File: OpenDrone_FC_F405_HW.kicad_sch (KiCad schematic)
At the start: 88 parts, among them J1 Conn_01x05, J11 Conn_01x05, J12 Conn_01x05, J13 Conn_01x02, J14 Conn_01x02, J16 Conn_01x05, J17 Conn_02x03_Odd_Even, J2 Conn_01x02, J3 Conn_01x02, J4 Conn_01x02, J5 Conn_01x02, J6 Conn_01x08, J7 Conn_01x02, J8 Conn_01x04, J9 Conn_01x02, U1 STM32F405RGTx, U2 TPS54331, U4 MPU6000, U5 HMC5883L, U6 BMP280, U7 TPS54331, U8 Board, Y2 8Mhz

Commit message: update project
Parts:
- added R18: 10k, Resistor_SMD:R_0402_1005Metric, symbol Device:R_Small
- added R19: 470R, Resistor_SMD:R_0402_1005Metric, symbol Device:R_Small
- R14: value 10k -> 0R
- R15: value 3.24k -> 3,3k
- R3: value 10k -> 4,7k
- R5: value 3.24k -> 1k
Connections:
- net 3V3_STEPDOWN: now also R18.2; no longer R14.1
- net 5V_STEPDOWN: now also R19.2; no longer R3.1
- net at R15.1, U2.5 (VSENSE): now also R14.1; no longer R14.2
- net at R5.1, U7.5 (VSENSE): now also R3.1; no longer R3.2
- new net: R14.2, R18.1
- new net: R19.1, R3.2
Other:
- moved on the sheet: C13, C14, C15, C16, C17, C39, C40, C41, D4, J17, L2, R13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

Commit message: update project
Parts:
- removed C20: 100nF, Capacitor_SMD:C_0402_1005Metric, symbol Device:C_Small
- removed C21: 2.2nF, Capacitor_SMD:C_0402_1005Metric, symbol Device:C_Small
- removed J11, J12, J16: Conn_01x05, Footprint:Header_1x05_P2.00mm_Vertical, symbol Connector_Generic:Conn_01x05
- removed J13, J14, J2, J3, J4, J5, J7, J9: Conn_01x02, Footprint:HolePad_1x2, symbol Connector_Generic:Conn_01x02
- removed U4: MPU6000, Footprint:QFN-24-1EP_4x4mm_P0.5mm_EP2.15x2.15mm, symbol MPU6000:MPU6000
- added C8: 10uF, Capacitor_SMD:C_0402_1005Metric, symbol Device:C_Small
- added J10, J11, J12: Conn_01x06, Footprint:Header_1x06_P2.00mm_Vertical, symbol Connector_Generic:Conn_01x06
- added U3: ICM42688, Package_LGA:LGA-14_3x2.5mm_P0.5mm_LayoutBorder3x4y, symbol ICM42688:ICM42688
- C19: value 10nF -> 10uF
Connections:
- net MPU6000_XCL is gone; now on net I2C2_SCL: U5.1 (SCL)
- net MPU6000_XDA is gone; now on net I2C2_SDA: U5.16 (SDA)
- net +3V3: now also R8.2, R9.1, C8.1, J10.6 (Pin_6), U3.5 (VDDIO), U3.8 (VDD); no longer R8.1
- net +5V: now also J12.6 (Pin_6)
- net GND: now also U6.5 (SDO), C8.2, J11.6 (Pin_6), U3.11 (RESV), U3.6 (GND), U3.7 (RESV); no longer R9.2
- net I2C1_SCL: now also J11.2 (Pin_2)
- net I2C1_SDA: now also J11.3 (Pin_3)
- net I2C2_SCL: now also R8.1; no longer R8.2
- net LED_STRIP1: now also J12.2 (Pin_2)
- net LED_STRIP2: now also J12.3 (Pin_3)
- net LORA_IRQ: no longer U1.45 (PA12)
- net LORA_RST: no longer U1.44 (PA11)
- net SPI1_CLK: now also U3.13 (SCL/SCLK)
- net SPI1_CS: now also U3.12 (CS)
- net SPI1_MISO: now also U3.1 (SDO/AD0)
- net SPI1_MOSI: now also U3.14 (SDA/SDIO/SDI)
- net SPI2_CLK: now also J10.5 (Pin_5)
- net SPI2_MISO: now also J10.4 (Pin_4)
- net SPI2_MOSI: now also J10.3 (Pin_3)
- net UART4_RX: now also J12.5 (Pin_5)
- net UART4_TX: now also J12.4 (Pin_4)
- net UART6_RX: now also J10.1 (Pin_1)
- net UART6_TX: now also J10.2 (Pin_2)
- net at U6.2 (CSB): now also R9.2
- net SPI2_CS1: now reaches U1.39 (PC8)
- net SPI2_CS1: now also J11.4 (Pin_4)
- net MPU6000_INT renamed ICM42688_INT
- net ICM42688_INT: now also U3.4 (INT1/INT)
- net SPI2_CS renamed SPI2_CS2
- net SPI2_CS2: now also J11.5 (Pin_5)
- no-connect marks 6 -> 8
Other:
- note added: "ICM42688"
- note added: "QMC5883L"
- note removed: "HMC5883L"
- note removed: "MPU6050"
- moved on the sheet: C18, C22, C23, C24, C25, C26, J6, J8, R7, R8, R9, U5

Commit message: update routing
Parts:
- removed D6: GREEN, LED_SMD:LED_0402_1005Metric, symbol Device:LED_Small
- removed R25: 470R, Resistor_SMD:R_0402_1005Metric, symbol Device:R_Small
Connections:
- net LED_BLUE: no longer names the net of U1.57 (PB5)

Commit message: update routing
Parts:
- U3: footprint Package_LGA:LGA-14_3x2.5mm_P0.5mm_LayoutBorder3x4y -> Footprint:LGA-14_3x2.5mm_P0.5mm
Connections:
- net PC9: now reaches U1.40 (PC9)
- net PC9: now also J11.1 (Pin_1)
- net PA8: now reaches U1.41 (PA8)
- net PA8: now also J12.1 (Pin_1)
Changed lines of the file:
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@@
 		)
 	)
-	(global_label "LORA_RST"
+	(global_label "PC9"
 		(shape input)
-		(at 330.2 152.4 0)
+		(at 331.47 127 0)
 		(fields_autoplaced yes)
 		(effects
@@
 		)
 		(property "Intersheetrefs" "${INTERSHEET_REFS}"
-			(at 342.3171 152.4 0)
+			(at 338.2047 127 0)
 			(effects
 				(font
@@
 		)
 	)
+	(global_label "PC9"
+		(shape input)
+		(at 45.72 93.98 180)
+		(fields_autoplaced yes)
+		(effects
+			(font
+				(size 1.27 1.27)
+			)
+			(justify right)
+		)
+		(property "Intersheetrefs" "${INTERSHEET_REFS}"
+			(at 38.9853 93.98 0)
+			(effects
+				(font
+					(size 1.27 1.27)
+				)
+				(justify right)
+				(hide yes)
+			)
+		)
+	)
 	(global_label "I2C1_SCL"
 		(shape input)
@@
 		)
 	)
-	(global_label "LORA_RST"
-		(shape input)
-		(at 85.09 76.2 0)
-		(fields_autoplaced yes)
-		(effects
-			(font
-				(size 1.27 1.27)
-			)
-			(justify left)
-		)
-		(property "Intersheetrefs" "${INTERSHEET_REFS}"
-			(at 97.2071 76.2 0)
-			(effects
-				(font
-					(size 1.27 1.27)
-				)
-				(justify left)
-				(hide yes)
-			)
-		)
-	)
 	(global_label "SPI2_CLK"
 		(shape input)
@@
 		)
 	)
-	(global_label "LORA_IRQ"
+	(global_label "PA8"
 		(shape input)
-		(at 330.2 149.86 0)
+		(at 363.22 125.73 0)
 		(fields_autoplaced yes)
 		(effects
@@
 		)
 		(property "Intersheetrefs" "${INTERSHEET_REFS}"
-			(at 342.0753 149.86 0)
+			(at 369.7733 125.73 0)
+			(effects
+				(font
+					(size 1.27 1.27)
+				)
+				(justify left)
+				(hide yes)
+			)
+		)
+	)
+	(global_label "PA8"
+		(shape input)
+		(at 81.28 68.58 0)
+		(fields_autoplaced yes)
+		(effects
+			(font
+				(size 1.27 1.27)
+			)
+			(justify left)
+		)
+		(property "Intersheetrefs" "${INTERSHEET_REFS}"
+			(at 87.8333 68.58 0)
 			(effects
 				(font
@@
 		)
 	)
-	(global_label "LORA_IRQ"
-		(shape input)
-		(at 85.09 78.74 0)
-		(fields_autoplaced yes)
-		(effects
-			(font
-				(size 1.27 1.27)
-			)
-			(justify left)
-		)
-		(property "Intersheetrefs" "${INTERSHEET_REFS}"
-			(at 96.9653 78.74 0)
-			(effects
-				(font
-					(size 1.27 1.27)
-				)
-				(justify left)
-				(hide yes)
-			)
-		)
-	)
 	(global_label "5V_STEPDOWN"
 		(shape input)
@@
 			)
 		)
-		(property "Footprint" "Package_LGA:LGA-14_3x2.5mm_P0.5mm_LayoutBorder3x4y"
+		(property "Footprint" "Footprint:LGA-14_3x2.5mm_P0.5mm"
 			(at 152.4 73.66 0)
 			(effects

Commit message: update setting
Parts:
- J6: footprint Footprint:Connector_XH_1x08_P1.25mm_Horizontal -> KiCad-Lib:Connector_XH_1x08_P1.25mm_Horizontal
- U3: footprint Footprint:LGA-14_3x2.5mm_P0.5mm -> KiCad-Lib:LGA-14_3x2.5mm_P0.5mm
- U5: footprint Footprint:QFN-16_3x3mm_P0.5mm -> KiCad-Lib:QFN-16_3x3mm_P0.5mm
- U6: footprint Footprint:LGA-8_2x2.5mm_P0.65mm -> KiCad-Lib:LGA-8_2x2.5mm_P0.65mm
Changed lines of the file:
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@@
 			)
 		)
-		(property "Footprint" "Footprint:LGA-8_2x2.5mm_P0.65mm"
+		(property "Footprint" "KiCad-Lib:LGA-8_2x2.5mm_P0.65mm"
 			(at 367.03 80.01 0)
 			(effects
@@
 			)
 		)
-		(property "Footprint" "Footprint:LGA-14_3x2.5mm_P0.5mm"
+		(property "Footprint" "KiCad-Lib:LGA-14_3x2.5mm_P0.5mm"
 			(at 152.4 73.66 0)
 			(effects
@@
 			)
 		)
-		(property "Footprint" "Footprint:QFN-16_3x3mm_P0.5mm"
+		(property "Footprint" "KiCad-Lib:QFN-16_3x3mm_P0.5mm"
 			(at 226.06 66.04 0)
 			(effects
@@
 			)
 		)
-		(property "Footprint" "Footprint:Connector_XH_1x08_P1.25mm_Horizontal"
+		(property "Footprint" "KiCad-Lib:Connector_XH_1x08_P1.25mm_Horizontal"
 			(at 304.8 105.41 0)
 			(effects

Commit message: update
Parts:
- J1: footprint Footprint:Connector_XH_1x05_P1.25mm_Horizontal -> KiCad-Lib:Connector_XH_1x05_P1.25mm_Horizontal
- J10, J11, J12: footprint Footprint:Header_1x06_P2.00mm_Vertical -> KiCad-Lib:Header_1x06_P2.00mm_Vertical
- J8: footprint Footprint:Connector_XH_1x04_P1.25mm_Horizontal -> KiCad-Lib:Connector_XH_1x04_P1.25mm_Horizontal
- L1, L2: footprint Footprint:Inductor_SMD_4D28 -> KiCad-Lib:Inductor_SMD_4D28
- U6: footprint KiCad-Lib:LGA-8_2x2.5mm_P0.65mm -> Package_LGA:Bosch_LGA-8_2x2.5mm_P0.65mm_ClockwisePinNumbering
- U8: footprint Footprint:Board_Outline_34x34_Hole_26x26 -> Proj-Lib:Board_Outline_34x34_Hole_26x26
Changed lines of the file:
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@@
 			)
 		)
-		(property "Footprint" "Footprint:Inductor_SMD_4D28"
+		(property "Footprint" "KiCad-Lib:Inductor_SMD_4D28"
 			(at 92.71 160.02 0)
 			(effects
@@
 			)
 		)
-		(property "Footprint" "Footprint:Inductor_SMD_4D28"
+		(property "Footprint" "KiCad-Lib:Inductor_SMD_4D28"
 			(at 209.55 161.29 0)
 			(effects
@@
 			)
 		)
-		(property "Footprint" "Footprint:Connector_XH_1x04_P1.25mm_Horizontal"
+		(property "Footprint" "KiCad-Lib:Connector_XH_1x04_P1.25mm_Horizontal"
 			(at 327.66 106.68 0)
 			(effects
@@
 			)
 		)
-		(property "Footprint" "Footprint:Header_1x06_P2.00mm_Vertical"
+		(property "Footprint" "KiCad-Lib:Header_1x06_P2.00mm_Vertical"
 			(at 295.91 132.08 0)
 			(effects
@@
 			)
 		)
-		(property "Footprint" "Footprint:Connector_XH_1x05_P1.25mm_Horizontal"
+		(property "Footprint" "KiCad-Lib:Connector_XH_1x05_P1.25mm_Horizontal"
 			(at 102.87 64.77 0)
 			(effects
@@
 			)
 		)
-		(property "Footprint" "KiCad-Lib:LGA-8_2x2.5mm_P0.65mm"
+		(property "Footprint" "Package_LGA:Bosch_LGA-8_2x2.5mm_P0.65mm_ClockwisePinNumbering"
 			(at 367.03 80.01 0)
 			(effects
@@
 			)
 		)
-		(property "Footprint" "Footprint:Board_Outline_34x34_Hole_26x26"
+		(property "Footprint" "Proj-Lib:Board_Outline_34x34_Hole_26x26"
 			(at 285.75 173.99 0)
 			(effects
@@
 			)
 		)
-		(property "Footprint" "Footprint:Header_1x06_P2.00mm_Vertical"
+		(property "Footprint" "KiCad-Lib:Header_1x06_P2.00mm_Vertical"
 			(at 326.39 132.08 0)
 			(effects
@@
 			)
 		)
-		(property "Footprint" "Footprint:Header_1x06_P2.00mm_Vertical"
+		(property "Footprint" "KiCad-Lib:Header_1x06_P2.00mm_Vertical"
 			(at 358.14 130.81 0)
 			(effects

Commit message: update routing
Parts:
- C1, C10, C13, C18, C19, C2, C22, C23, C24, C25, C26, C27, C28, C29, C3, C30, C31, C32, C33, C34, C35, C36, C37, C38, C39, C4, C40, C41, C5, C6, C7, C8, C9: footprint Capacitor_SMD:C_0402_1005Metric -> KiCad-Lib:C_0402_1005Metric
- C11, C12, C14, C15, C16, C17: footprint Capacitor_SMD:C_1210_3225Metric -> KiCad-Lib:C_1210_3225Metric
- D1, D4: footprint Diode_SMD:D_SMA -> KiCad-Lib:D_SMA
- D2, D3: footprint LED_SMD:LED_0402_1005Metric -> KiCad-Lib:LED_0402_1005Metric
- R1, R10, R11, R12, R13, R14, R15, R16, R17, R18, R19, R2, R3, R4, R5, R6, R7, R8, R9: footprint Resistor_SMD:R_0402_1005Metric -> KiCad-Lib:R_0402_1005Metric
- U2, U7: footprint Package_SO:SOIC-8-1EP_3.9x4.9mm_P1.27mm_EP2.29x3mm -> KiCad-Lib:SOIC-8-1EP_3.9x4.9mm_P1.27mm_EP2.29x3mm
- U6: footprint Package_LGA:Bosch_LGA-8_2x2.5mm_P0.65mm_ClockwisePinNumbering -> KiCad-Lib:LGA-8_2x2.5mm_P0.65mm
- Y2: footprint Crystal:Crystal_SMD_3225-4Pin_3.2x2.5mm -> KiCad-Lib:Crystal_SMD_3225-4Pin_3.2x2.5mm

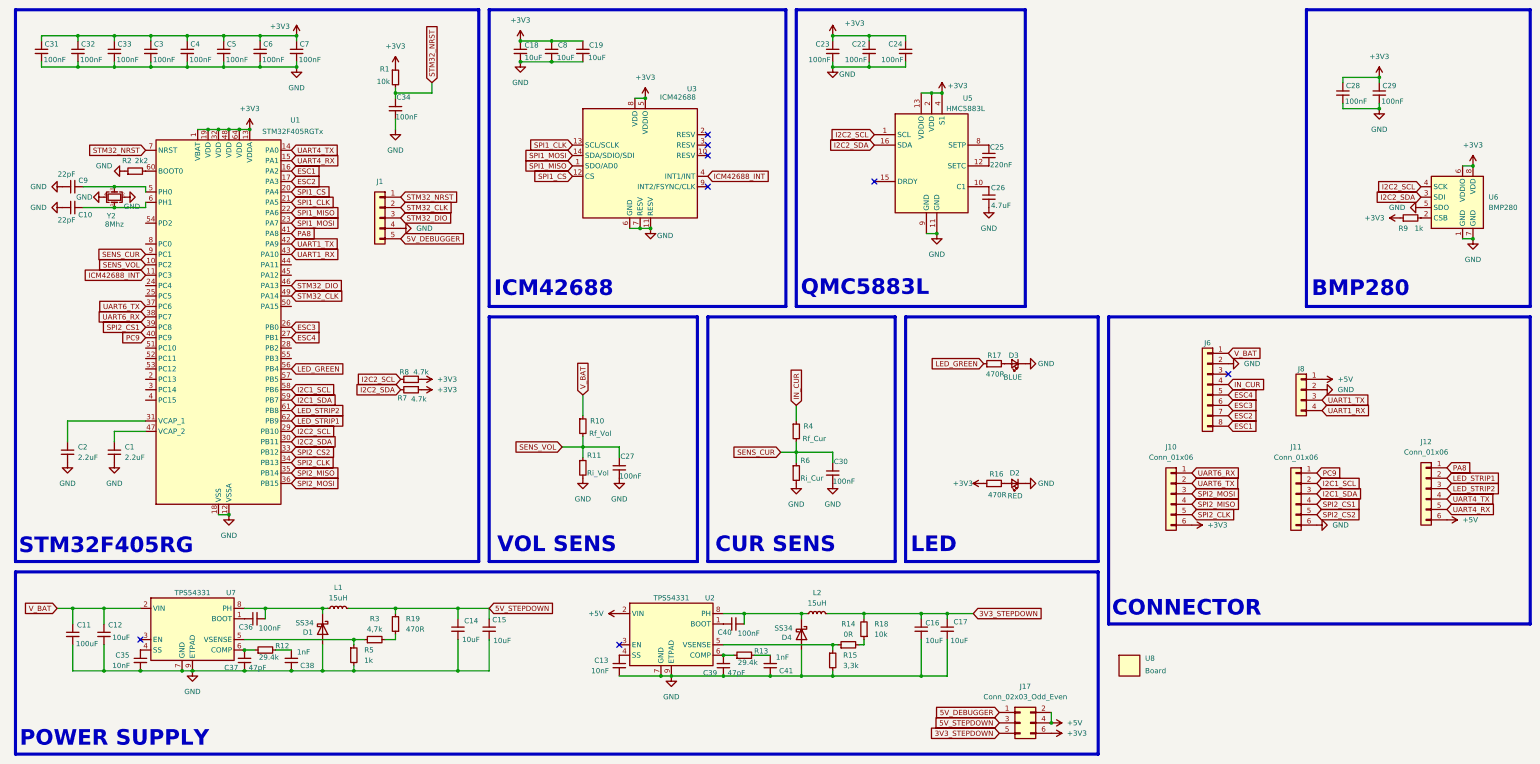
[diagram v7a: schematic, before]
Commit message: update schematic
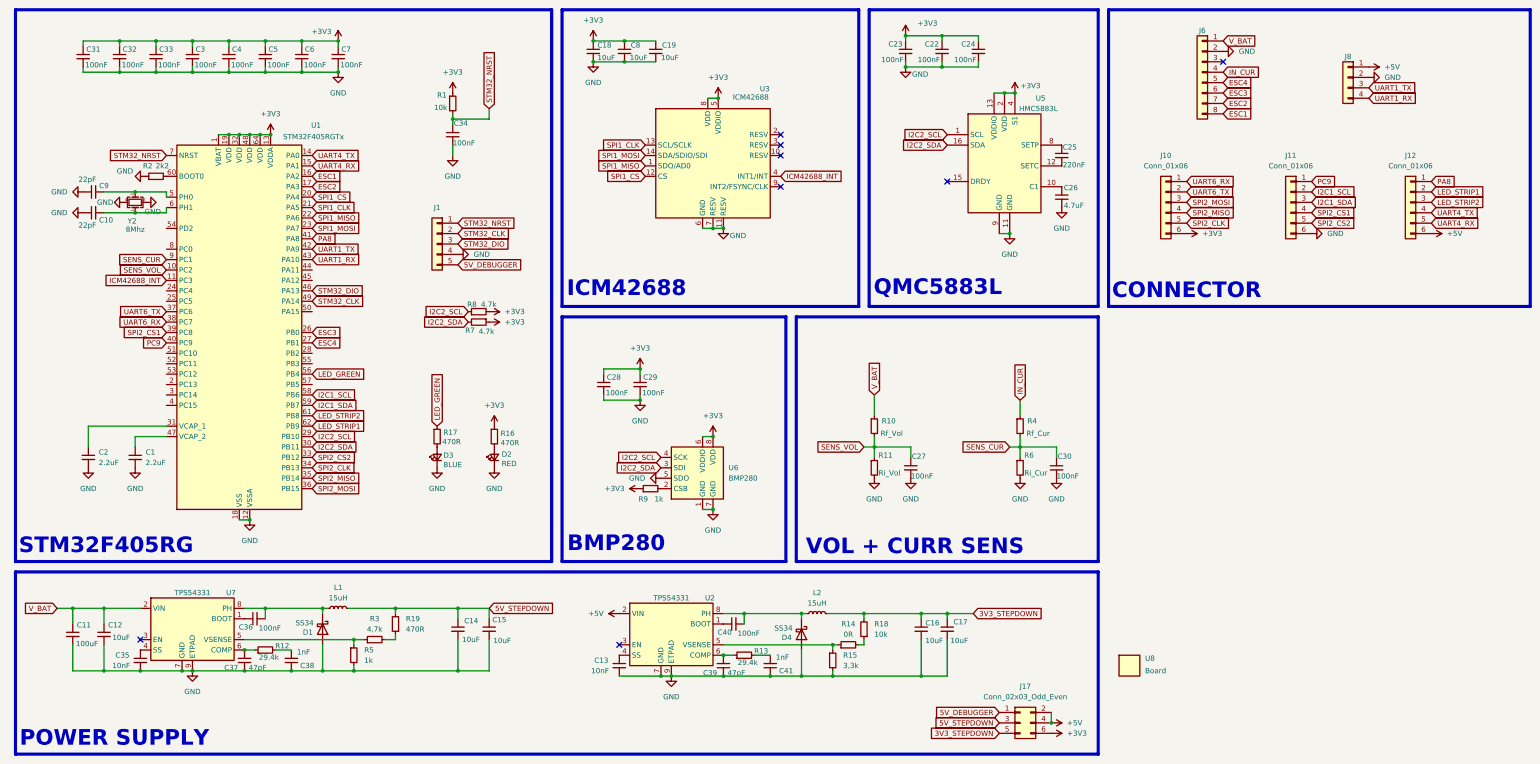
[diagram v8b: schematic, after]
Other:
- note added: "VOL + CURR SENS"
- note removed: "CUR SENS"
- note removed: "LED"
- note removed: "VOL SENS"
- moved on the sheet: C1, C10, C18, C19, C2, C22, C23, C24, C25, C26, C27, C28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
